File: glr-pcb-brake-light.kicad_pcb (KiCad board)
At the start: 2 copper layers, 126 x 30 mm, 38 parts, among them J1 Conn_01x04_Pin

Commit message: final version
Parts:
- R5: moved to B.Cu
- moved D31 210.7 mm to (214.9, 94.1), turned to 180 degrees
- moved D30 193.5 mm to (197.9, 94.1), turned to 180 degrees
- moved D29 176.4 mm to (180.9, 94.1), turned to 180 degrees
- moved D28 144.8 mm to (146.7, 94.1), turned to 180 degrees
- moved R5 130.7 mm to (140.0, 89.7)
- moved D27 128.3 mm to (129.7, 94.1), turned to 180 degrees
- moved D26 112.1 mm to (112.7, 94.1), turned to 180 degrees
- moved R3 9.26 mm to (126.9, 99.0)
- moved R1 8.76 mm to (126.9, 89.7)
- moved R2 7.10 mm to (179.6, 90.7)
- moved R4 7.10 mm to (179.6, 97.8)
- moved D0 3.51 mm to (141.3, 99.0)
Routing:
- net Net-(D0-K): track 0.00 -> 74.2 mm
- net Net-(D26-A): track 0.00 -> 40.0 mm, vias 0 -> 1
- net Net-(D28-K): track 0.00 -> 31.2 mm
- net Net-(D13-A): track 0.00 -> 26.6 mm, vias 0 -> 1
- net Net-(D1-A): track 0.00 -> 23.6 mm, vias 0 -> 1
- net Net-(D19-A): track 0.00 -> 21.0 mm, vias 0 -> 1
- net +24V: track 0.00 -> 20.5 mm
- net Net-(D7-A): track 0.00 -> 19.0 mm, vias 0 -> 1
- net Net-(D30-K): track 0.00 -> 14.0 mm
- net Net-(D29-K): track 0.00 -> 14.0 mm
- net Net-(D27-K): track 0.00 -> 14.0 mm
- net Net-(D26-K): track 0.00 -> 14.0 mm

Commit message: mounting holes hinzugefügt
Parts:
- added REF**: MountingHole_3.2mm_M3, MountingHole:MountingHole_3.2mm_M3, F.Cu at (221.9, 95.3)
- added REF**: MountingHole_3.2mm_M3, MountingHole:MountingHole_3.2mm_M3, F.Cu at (105.1, 95.3)
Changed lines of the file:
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@@
 		)
 	)
+	(footprint "MountingHole:MountingHole_3.2mm_M3"
+		(layer "F.Cu")
+		(at 221.918 95.309)
+		(descr "Mounting Hole 3.2mm, M3, no annular, generated by kicad-footprint-generator mountinghole.py")
+		(tags "mountinghole M3")
+		(property "Reference" "REF**"
+			(at 0 -4.15 0)
+			(layer "F.SilkS")
+			(effects
+				(font
+					(size 1 1)
+					(thickness 0.15)
+				)
+			)
+		)
+		(property "Value" "MountingHole_3.2mm_M3"
+			(at 0 4.15 0)
+			(layer "F.Fab")
+			(effects
+				(font
+					(size 1 1)
+					(thickness 0.15)
+				)
+			)
+		)
+		(property "Datasheet" ""
+			(at 0 0 0)
+			(layer "F.Fab")
+			(hide yes)
+			(effects
+				(font
+					(size 1.27 1.27)
+				)
+			)
+		)
+		(property "Description" ""
+			(at 0 0 0)
+			(layer "F.Fab")
+			(hide yes)
+			(effects
+				(font
+					(size 1.27 1.27)
+				)
+			)
+		)
+		(property "KiLib_Generator" "mounting_hardware/mounting_hole"
+			(at 0 0 0)
+			(layer "F.SilkS")
+			(hide yes)
+			(effects
+				(font
+					(size 1 1)
+					(thickness 0.15)
+				)
+			)
+		)
+		(attr exclude_from_pos_files exclude_from_bom)
+		(duplicate_pad_numbers_are_jumpers no)
+		(fp_circle
+			(center 0 0)
+			(end 3.2 0)
+			(stroke
+				(width 0.15)
+				(type solid)
+			)
+			(fill no)
+			(layer "Cmts.User")
+		)
+		(fp_circle
+			(center 0 0)
+			(end 3.45 0)
+			(stroke
+				(width 0.05)
+				(type solid)
+			)
+			(fill no)
+			(layer "F.CrtYd")
+		)
+		(fp_text user "${REFERENCE}"
+			(at 0 0 0)
+			(layer "F.Fab")
+			(effects
+				(font
+					(size 1 1)
+					(thickness 0.15)
+				)
+			)
+		)
+		(pad "" np_thru_hole circle
+			(at 0 0)
+			(size 3.2 3.2)
+			(drill 3.2)
+			(layers "*.Cu" "*.Mask")
+		)
+		(embedded_fonts no)
+	)
 	(footprint "GLR_KiCad_Library:LED_Avago_PLCC4_3.2x2.8mm_CW"
 		(layer "F.Cu")
@@
 		)
 	)
+	(footprint "MountingHole:MountingHole_3.2mm_M3"
+		(layer "F.Cu")
+		(at 105.117 95.309)
+		(descr "Mounting Hole 3.2mm, M3, no annular, generated by kicad-footprint-generator mountinghole.py")
+		(tags "mountinghole M3")
+		(property "Reference" "REF**"
+			(at 0 -4.15 0)
+			(layer "F.SilkS")
+			(effects
+				(font
+					(size 1 1)
+					(thickness 0.15)
+				)
+			)
+		)
+		(property "Value" "MountingHole_3.2mm_M3"
+			(at 0 4.15 0)
+			(layer "F.Fab")
+			(effects
+				(font
+					(size 1 1)
+					(thickness 0.15)
+				)
+			)
+		)
+		(property "Datasheet" ""
+			(at 0 0 0)
+			(layer "F.Fab")
+			(hide yes)
+			(effects
+				(font
+					(size 1.27 1.27)
+				)
+			)
+		)
+		(property "Description" ""
+			(at 0 0 0)
+			(layer "F.Fab")
+			(hide yes)
+			(effects
+				(font
+					(size 1.27 1.27)
+				)
+			)
+		)
+		(property "KiLib_Generator" "mounting_hardware/mounting_hole"
+			(at 0 0 0)
+			(layer "F.SilkS")
+			(hide yes)
+			(effects
+				(font
+					(size 1 1)
+					(thickness 0.15)
+				)
+			)
+		)
+		(attr exclude_from_pos_files exclude_from_bom)
+		(duplicate_pad_numbers_are_jumpers no)
+		(fp_circle
+			(center 0 0)
+			(end 3.2 0)
+			(stroke
+				(width 0.15)
+				(type solid)
+			)
+			(fill no)
+			(layer "Cmts.User")
+		)
+		(fp_circle
+			(center 0 0)
+			(end 3.45 0)
+			(stroke
+				(width 0.05)
+				(type solid)
+			)
+			(fill no)
+			(layer "F.CrtYd")
+		)
+		(fp_text user "${REFERENCE}"
+			(at 0 0 0)
+			(layer "F.Fab")
+			(effects
+				(font
+					(size 1 1)
+					(thickness 0.15)
+				)
+			)
+		)
+		(pad "" np_thru_hole circle
+			(at 0 0)
+			(size 3.2 3.2)
+			(drill 3.2)
+			(layers "*.Cu" "*.Mask")
+		)
+		(embedded_fonts no)
+	)
 	(footprint "GLR_KiCad_Library:LED_Avago_PLCC4_3.2x2.8mm_CW"
 		(layer "F.Cu")
@@
 	)
 	(gr_rect
-		(start 100.01 79.64)
-		(end 226.01 109.64)
+		(start 100.01 79.6413)
+		(end 226.010302 109.64)
 		(stroke
 			(width 0.05)
@@
 	)
 	(segment
-		(start 176.54 90.65)
-		(end 146.491 90.65)
-		(width 1)
-		(layer "B.Cu")
-		(net "Net-(D0-K)")
-	)
-	(segment
-		(start 139.29 97.851)
-		(end 139.29 98.99)
-		(width 1)
-		(layer "B.Cu")
-		(net "Net-(D0-K)")
-	)
-	(segment
-		(start 136.94 89.727)
-		(end 129.892 89.727)
-		(width 1)
-		(layer "B.Cu")
-		(net "Net-(D0-K)")
-	)
-	(segment
-		(start 129.892 98.952)
-		(end 129.93 98.99)
-		(width 1)
-		(layer "B.Cu")
-		(net "Net-(D0-K)")
-	)
-	(segment
-		(start 146.491 90.65)
-		(end 139.29 97.851)
-		(width 1)
-		(layer "B.Cu")
-		(net "Net-(D0-K)")
-	)
-	(segment
-		(start 129.93 98.99)
-		(end 129.93 89.727)
-		(width 1)
-		(layer "B.Cu")
-		(net "Net-(D0-K)")
-	)
-	(segment
-		(start 139.29 98.99)
-		(end 129.93 98.99)
-		(width 1)
-		(layer "B.Cu")
-		(net "Net-(D0-K)")
-	)
-	(segment
-		(start 176.54 97.75)
-		(end 176.54 90.65)
-		(width 1)
-		(layer "B.Cu")
-		(net "Net-(D0-K)")
-	)
-	(segment
 		(start 131.2 94.845)
 		(end 145.2 94.845)
@@
 	)
 	(segment
+		(start 176.54 90.65)
+		(end 146.491 90.65)
+		(width 1)
+		(layer "B.Cu")
+		(net "Net-(D0-K)")
+	)
+	(segment
+		(start 139.29 97.851)
+		(end 139.29 98.99)
+		(width 1)
+		(layer "B.Cu")
+		(net "Net-(D0-K)")
+	)
+	(segment
+		(start 136.94 89.727)
+		(end 129.892 89.727)
+		(width 1)
+		(layer "B.Cu")
+		(net "Net-(D0-K)")
+	)
+	(segment
+		(start 129.892 98.952)
+		(end 129.93 98.99)
+		(width 1)
+		(layer "B.Cu")
+		(net "Net-(D0-K)")
+	)
+	(segment
+		(start 146.491 90.65)
+		(end 139.29 97.851)
+		(width 1)
+		(layer "B.Cu")
+		(net "Net-(D0-K)")
+	)
+	(segment
+		(start 129.93 98.99)
+		(end 129.93 89.727)
+		(width 1)
+		(layer "B.Cu")
+		(net "Net-(D0-K)")
+	)
+	(segment
+		(start 139.29 98.99)
+		(end 129.93 98.99)
+		(width 1)
+		(layer "B.Cu")
+		(net "Net-(D0-K)")
+	)
+	(segment
+		(start 176.54 97.75)
+		(end 176.54 90.65)
+		(width 1)
+		(layer "B.Cu")
+		(net "Net-(D0-K)")
+	)
+	(segment

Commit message: letzte korrektur
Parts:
- moved G*** 0.89 mm to (213.2, 100.0)
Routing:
- net GND: track 9.00 -> 11.2 mm, vias 4 -> 5
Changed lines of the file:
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@@
 			(outputformat 1)
 			(mirror no)
-			(drillshape 1)
+			(drillshape 0)
 			(scaleselection 1)
-			(outputdirectory "")
+			(outputdirectory "C:/Users/elaka/Documents/GitHub/glr-pcb-brake-light/")
 		)
 	)
@@
 		(tags "LED Avago PLCC-4 3528 ASMB-MTB0-0A3A2")
 		(property "Reference" "D31"
-			(at 0 -2.65 0)
+			(at 0.294 -2.455 0)
 			(layer "F.SilkS")
 			(effects
@@
 	(footprint "GLR_KiCad_Library:glr-logo"
 		(layer "F.Cu")
-		(at 214.01 99.64)
+		(at 213.219 100.048)
 		(property "Reference" "G***"
 			(at 0 0 0)
@@
 	)
 	(segment
+		(start 216.404 94.926)
+		(end 216.404 97.176)
+		(width 0.5)
+		(layer "F.Cu")
+		(net "GND")
+	)
+	(segment
 		(start 160.11 84.3)
 		(end 162.36 84.3)
@@
 		(size 0.8)
 		(drill 0.4)
+		(layers "F.Cu" "B.Cu")
+		(free yes)
+		(net "GND")
+	)
+	(via
+		(at 216.404 97.176)
+		(size 0.8)
+		(drill 0.4)

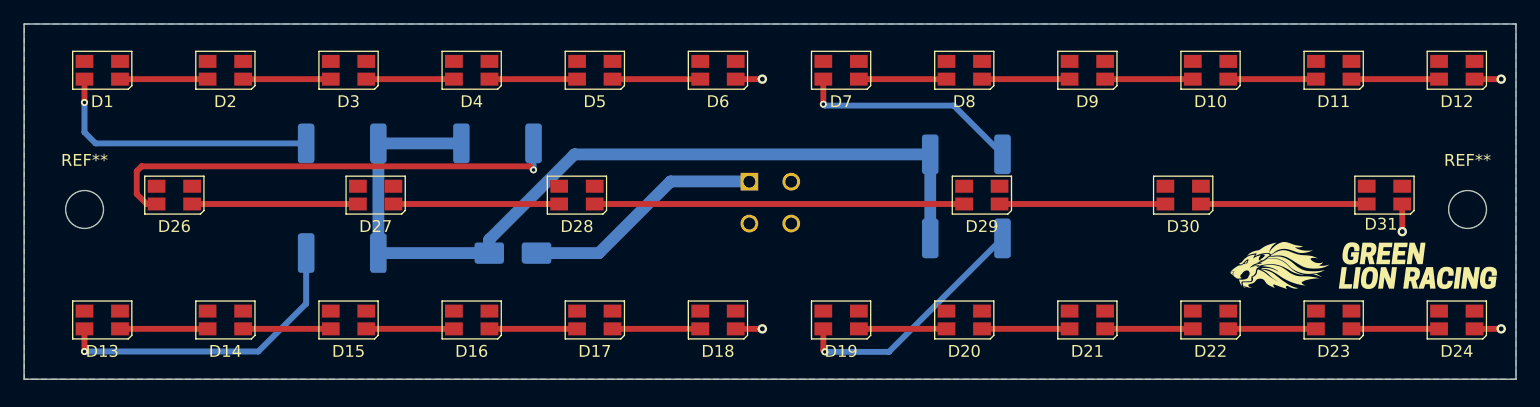
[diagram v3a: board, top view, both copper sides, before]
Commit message: improve positions
- align holes
- align leds to border
- make size exactly 125 x 30 mm
- remove temp files
- exclude production files
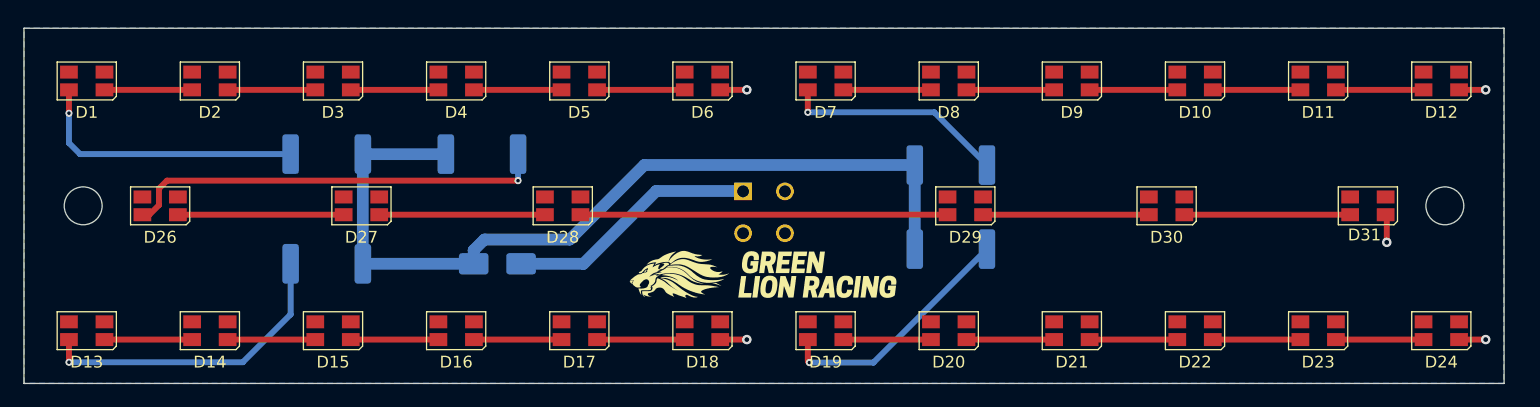
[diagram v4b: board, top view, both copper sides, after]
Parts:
- moved G*** 50.7 mm to (162.5, 100.8)
- moved REF** 1.94 mm to (220.0, 95.0)
- moved D29 1.67 mm to (179.5, 95.0)
- moved D30 1.67 mm to (196.5, 95.0)
- moved D31 1.67 mm to (213.5, 95.0)
- moved D0 1.59 mm to (140.0, 99.9)
- moved D1 1.59 mm to (105.3, 84.5)
- moved D10 1.59 mm to (198.9, 84.5)
- moved D11 1.59 mm to (209.3, 84.5)
- moved D12 1.59 mm to (219.7, 84.5)
- moved D13 1.59 mm to (105.3, 105.5)
- moved D14 1.59 mm to (115.7, 105.5)
- moved D15 1.59 mm to (126.1, 105.5)
- moved D16 1.59 mm to (136.5, 105.5)
- moved D17 1.59 mm to (146.9, 105.5)
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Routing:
- net Net-(D26-A): track 40.0 -> 36.1 mm
- net +24V: track 20.5 -> 22.1 mm
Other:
- board size 126 x 30 mm -> 125 x 30 mm
